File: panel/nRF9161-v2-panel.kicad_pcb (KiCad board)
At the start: 4 copper layers, 118 x 93 mm, 474 parts, among them J2 U.FL_LTE_NR+, J20 HOST_1x10_2.54, J5 U.FL_GNSS, J7 nanoSIM_4FF, J8 SWD_10pin, Q1 BSS138, SW2 RESET, U1 NRF9161-LACA-R7, U2 TLV73333PDBV, U3 TPS22919DCKR, U4 TPD3F303DPV, U5 SN74LXC2T45, U6 SN74LXC2T45, U7 SN74LXC1T45, U8 SN74LXC1T45

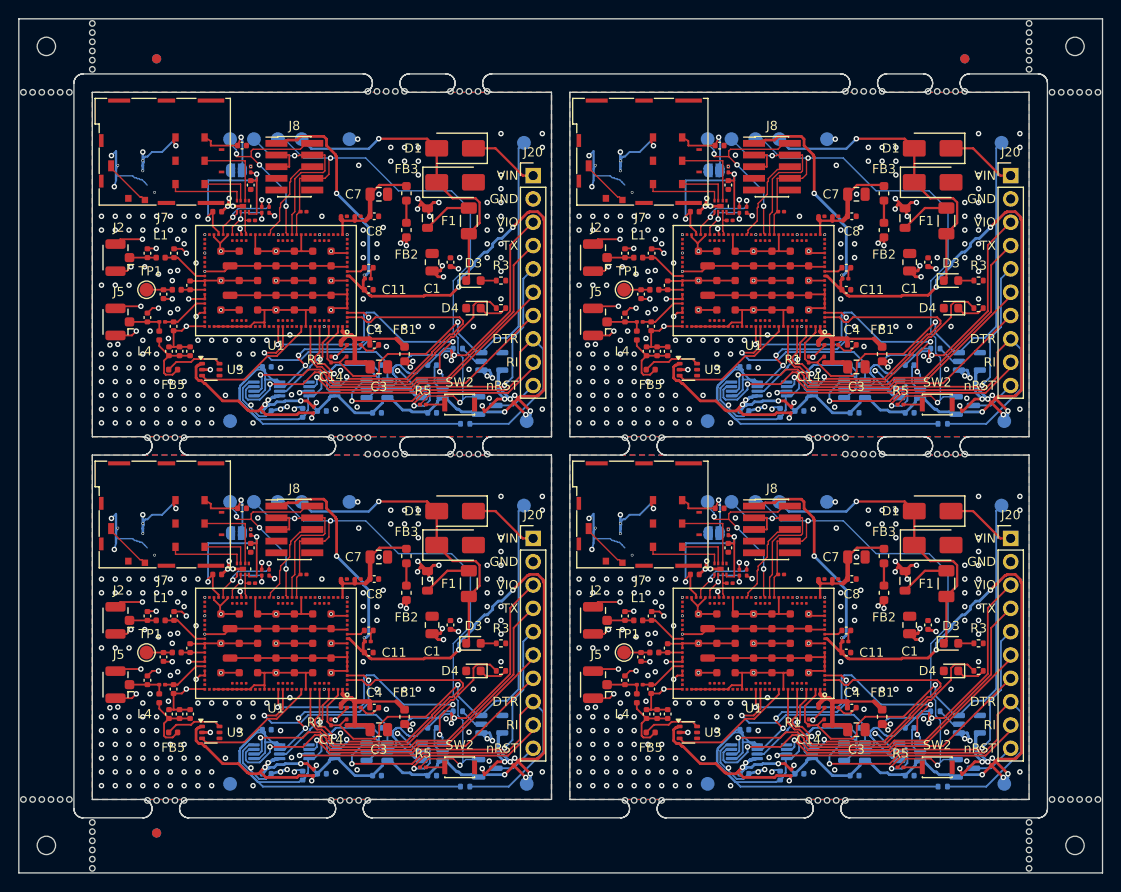
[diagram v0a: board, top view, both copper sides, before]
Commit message: v2f-5: panel regenerated (KiKit 1.8.1, v2_panel.json, same N/S tab positions) from rounded-corner board; 128 mousebite holes; panel DRC 0 errors / 0 unconnected
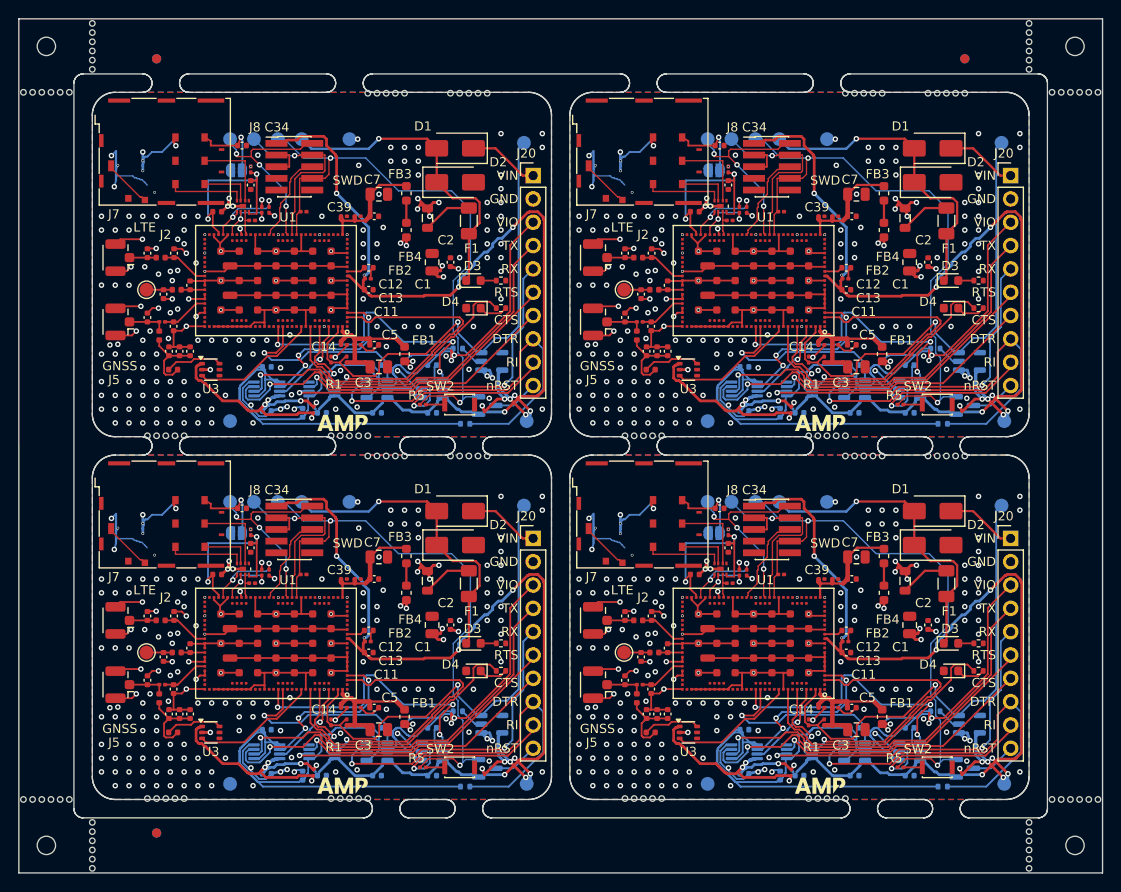
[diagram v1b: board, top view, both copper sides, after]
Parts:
- removed the C44 at (174.5, 102.2)
- removed the C44 at (174.5, 62.7)
- removed the C44 at (122.5, 62.7)
- removed the C44 at (122.5, 102.2)
- added C44: 100nF, Capacitor_SMD:C_0402_1005Metric, B.Cu at (174.5, 62.9)
- added C44: 100nF, Capacitor_SMD:C_0402_1005Metric, B.Cu at (122.5, 62.9)
- added C44: 100nF, Capacitor_SMD:C_0402_1005Metric, B.Cu at (174.5, 102.4)
- added C44: 100nF, Capacitor_SMD:C_0402_1005Metric, B.Cu at (122.5, 102.4)
- moved KiKit_MB_1_1 50.0 mm to (103.5, 65.4)
- moved KiKit_MB_1_2 50.0 mm to (104.5, 65.4)
- moved KiKit_MB_1_3 50.0 mm to (105.5, 65.4)
- moved KiKit_MB_1_4 50.0 mm to (106.5, 65.4)
- moved KiKit_MB_1_5 50.0 mm to (107.5, 65.4)
- moved KiKit_MB_5_1 50.0 mm to (155.5, 65.4)
- moved KiKit_MB_5_2 50.0 mm to (156.5, 65.4)
- moved KiKit_MB_5_3 50.0 mm to (157.5, 65.4)
- moved KiKit_MB_5_4 50.0 mm to (158.5, 65.4)
- moved KiKit_MB_5_5 50.0 mm to (159.5, 65.4)
- moved KiKit_MB_10_1 50.0 mm to (140.5, 67.6)
- moved KiKit_MB_10_2 50.0 mm to (139.5, 67.6)
- moved KiKit_MB_10_3 50.0 mm to (138.5, 67.6)
- moved KiKit_MB_10_4 50.0 mm to (137.5, 67.6)
- moved KiKit_MB_10_5 50.0 mm to (136.5, 67.6)
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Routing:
- net Board_3-GND: vias 188 -> 179
- net Board_2-GND: vias 188 -> 179
- net Board_1-GND: vias 188 -> 179
- net Board_0-GND: vias 188 -> 179
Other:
- outline, holes or cut-outs redrawn
- board text added: "GNSS"
- board text added: "LTE"
- board text added: "SWD"
- board text added: "nRF9161 UART Modem v2"
